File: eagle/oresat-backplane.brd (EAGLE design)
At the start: 82 x 213.6 mm, 98 parts

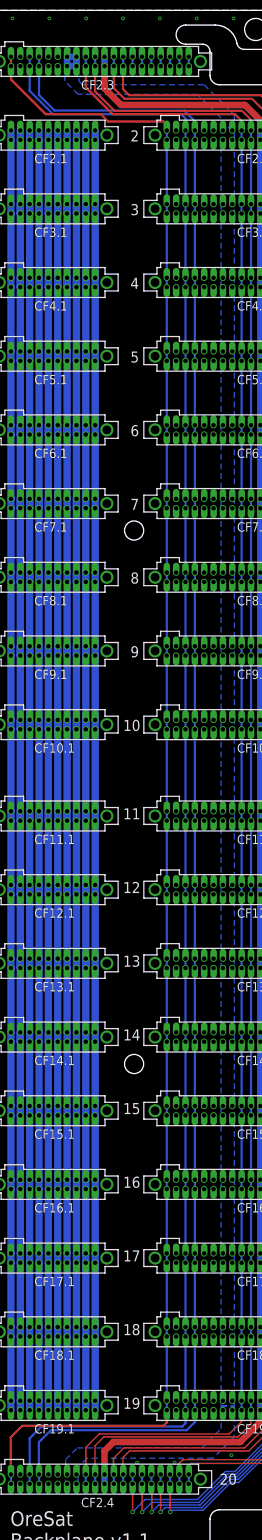
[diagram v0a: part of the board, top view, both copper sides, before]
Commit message: Fixed wrong signal names, removed thermals from bottom of main connectors, should be ready for fab.
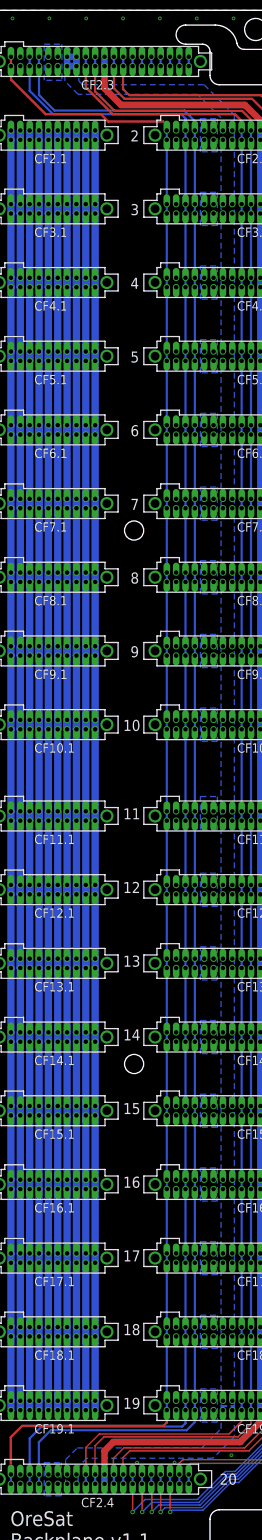
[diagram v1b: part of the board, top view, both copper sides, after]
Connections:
- net MAIN-1 renamed SPARE7
- net MAIN-2 renamed SPARE6
- net MAIN-3 renamed SPARE5
- net MAIN-4 renamed SPARE4
- net MAIN-5 renamed SPARE3
- net MAIN-6 renamed SPARE2
- net MAIN-7 renamed SPARE1
- net PE_PWR renamed OPD_PWR
- net PE_SCL renamed OPD_SCL
- net PE_SDA renamed OPD_SDA
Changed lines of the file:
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@@
 <?xml version="1.0" encoding="utf-8"?>
 <!DOCTYPE eagle SYSTEM "eagle.dtd">
-<eagle version="9.2.2">
+<eagle version="9.3.0">
 <drawing>
 <settings>
-<setting alwaysvectorfont="no"/>
+<setting alwaysvectorfont="yes"/>
 <setting keepoldvectorfont="yes"/>
 <setting verticaltext="up"/>
 </settings>
-<grid distance="1" unitdist="mm" unit="mm" style="lines" multiple="1" display="yes" altdistance="0.025" altunitdist="inch" altunit="inch"/>
+<grid distance="0.1" unitdist="mm" unit="mm" style="lines" multiple="1" display="yes" altdistance="0.025" altunitdist="inch" altunit="inch"/>
 <layers>
-<layer number="1" name="Top" color="4" fill="1" visible="no" active="yes"/>
+<layer number="1" name="Top" color="4" fill="1" visible="yes" active="yes"/>
 <layer number="2" name="Route2" color="1" fill="3" visible="no" active="no"/>
 <layer number="3" name="Route3" color="4" fill="3" visible="no" active="no"/>
@@
 <layer number="14" name="Route14" color="1" fill="6" visible="no" active="no"/>
 <layer number="15" name="Route15" color="4" fill="6" visible="no" active="no"/>
-<layer number="16" name="Bottom" color="1" fill="1" visible="yes" active="yes"/>
+<layer number="16" name="Bottom" color="1" fill="1" visible="no" active="yes"/>
 <layer number="17" name="Pads" color="2" fill="1" visible="yes" active="yes"/>
 <layer number="18" name="Vias" color="2" fill="1" visible="yes" active="yes"/>
 <layer number="19" name="Unrouted" color="6" fill="1" visible="yes" active="yes"/>
 <layer number="20" name="Dimension" color="24" fill="1" visible="yes" active="yes"/>
-<layer number="21" name="tPlace" color="7" fill="1" visible="no" active="yes"/>
-<layer number="22" name="bPlace" color="7" fill="1" visible="yes" active="yes"/>
-<layer number="23" name="tOrigins" color="15" fill="1" visible="no" active="yes"/>
-<layer number="24" name="bOrigins" color="15" fill="1" visible="yes" active="yes"/>
-<layer number="25" name="tNames" color="7" fill="1" visible="no" active="yes"/>
-<layer number="26" name="bNames" color="7" fill="1" visible="yes" active="yes"/>
+<layer number="21" name="tPlace" color="7" fill="1" visible="yes" active="yes"/>
+<layer number="22" name="bPlace" color="7" fill="1" visible="no" active="yes"/>
+<layer number="23" name="tOrigins" color="15" fill="1" visible="yes" active="yes"/>
+<layer number="24" name="bOrigins" color="15" fill="1" visible="no" active="yes"/>
+<layer number="25" name="tNames" color="7" fill="1" visible="yes" active="yes"/>
+<layer number="26" name="bNames" color="7" fill="1" visible="no" active="yes"/>
 <layer number="27" name="tValues" color="7" fill="1" visible="no" active="yes"/>
 <layer number="28" name="bValues" color="7" fill="1" visible="no" active="yes"/>
-<layer number="29" name="tStop" color="7" fill="3" visible="no" active="yes"/>
-<layer number="30" name="bStop" color="7" fill="6" visible="yes" active="yes"/>
+<layer number="29" name="tStop" color="7" fill="3" visible="yes" active="yes"/>
+<layer number="30" name="bStop" color="7" fill="6" visible="no" active="yes"/>
 <layer number="31" name="tCream" color="7" fill="4" visible="no" active="yes"/>
 <layer number="32" name="bCream" color="7" fill="5" visible="no" active="yes"/>
@@
 <via x="1" y="103" extent="1-16" drill="0.254"/>
 <via x="1" y="109" extent="1-16" drill="0.254"/>
+<polygon width="0.2" layer="16" isolate="0.2" thermals="no">
+<vertex x="12.3" y="209"/>
+<vertex x="14.7" y="209"/>
+<vertex x="14.7" y="204.1"/>
+<vertex x="12.3" y="204.1"/>
+</polygon>
+<polygon width="0.2" layer="16" isolate="0.2" thermals="no">
+<vertex x="33.5" y="198.9"/>
+<vertex x="35.8" y="198.9"/>
+<vertex x="35.8" y="194.4"/>
+<vertex x="33.5" y="194.4"/>
+</polygon>
+<polygon width="0.2" layer="16" isolate="0.2" thermals="no">
+<vertex x="33.5" y="188.9"/>
+<vertex x="35.8" y="188.9"/>
+<vertex x="35.8" y="184.4"/>
+<vertex x="33.5" y="184.4"/>
+</polygon>
+<polygon width="0.2" layer="16" isolate="0.2" thermals="no">
+<vertex x="33.5" y="178.9"/>
+<vertex x="35.8" y="178.9"/>
+<vertex x="35.8" y="174.4"/>
+<vertex x="33.5" y="174.4"/>
+</polygon>
+<polygon width="0.2" layer="16" isolate="0.2" thermals="no">
+<vertex x="33.5" y="168.9"/>
+<vertex x="35.8" y="168.9"/>
+<vertex x="35.8" y="164.4"/>
+<vertex x="33.5" y="164.4"/>
+</polygon>
+<polygon width="0.2" layer="16" isolate="0.2" thermals="no">
+<vertex x="33.5" y="158.9"/>
+<vertex x="35.8" y="158.9"/>
+<vertex x="35.8" y="154.4"/>
+<vertex x="33.5" y="154.4"/>
+</polygon>
+<polygon width="0.2" layer="16" isolate="0.2" thermals="no">
+<vertex x="33.5" y="148.9"/>
+<vertex x="35.8" y="148.9"/>
+<vertex x="35.8" y="144.4"/>
+<vertex x="33.5" y="144.4"/>
+</polygon>
+<polygon width="0.2" layer="16" isolate="0.2" thermals="no">
+<vertex x="33.5" y="138.9"/>
+<vertex x="35.8" y="138.9"/>
+<vertex x="35.8" y="134.4"/>
+<vertex x="33.5" y="134.4"/>
+</polygon>
+<polygon width="0.2" layer="16" isolate="0.2" thermals="no">
+<vertex x="33.5" y="128.9"/>
+<vertex x="35.8" y="128.9"/>
+<vertex x="35.8" y="124.4"/>
+<vertex x="33.5" y="124.4"/>
+</polygon>
+<polygon width="0.2" layer="16" isolate="0.2" thermals="no">
+<vertex x="33.5" y="118.9"/>
+<vertex x="35.8" y="118.9"/>
+<vertex x="35.8" y="114.4"/>
+<vertex x="33.5" y="114.4"/>
+</polygon>
+<polygon width="0.2" layer="16" isolate="0.2" thermals="no">
+<vertex x="33.5" y="106.9"/>
+<vertex x="35.8" y="106.9"/>
+<vertex x="35.8" y="102.4"/>
+<vertex x="33.5" y="102.4"/>
+</polygon>
+<polygon width="0.2" layer="16" isolate="0.2" thermals="no">
+<vertex x="33.5" y="96.5"/>
+<vertex x="35.8" y="96.5"/>
+<vertex x="35.8" y="92"/>
+<vertex x="33.5" y="92"/>
+</polygon>
+<polygon width="0.2" layer="16" isolate="0.2" thermals="no">
+<vertex x="33.5" y="86.5"/>
+<vertex x="35.8" y="86.5"/>
+<vertex x="35.8" y="82"/>
+<vertex x="33.5" y="82"/>
+</polygon>
+<polygon width="0.2" layer="16" isolate="0.2" thermals="no">
+<vertex x="33.5" y="76.5"/>
+<vertex x="35.8" y="76.5"/>
+<vertex x="35.8" y="72"/>
+<vertex x="33.5" y="72"/>
+</polygon>
+<polygon width="0.2" layer="16" isolate="0.2" thermals="no">
+<vertex x="33.5" y="66.5"/>
+<vertex x="35.8" y="66.5"/>
+<vertex x="35.8" y="62"/>
+<vertex x="33.5" y="62"/>
+</polygon>
+<polygon width="0.2" layer="16" isolate="0.2" thermals="no">
+<vertex x="33.5" y="56.5"/>
+<vertex x="35.8" y="56.5"/>
+<vertex x="35.8" y="52"/>
+<vertex x="33.5" y="52"/>
+</polygon>
+<polygon width="0.2" layer="16" isolate="0.2" thermals="no">
+<vertex x="33.5" y="46.5"/>
+<vertex x="35.8" y="46.5"/>
+<vertex x="35.8" y="42"/>
+<vertex x="33.5" y="42"/>
+</polygon>
+<polygon width="0.2" layer="16" isolate="0.2" thermals="no">
+<vertex x="33.5" y="36.5"/>
+<vertex x="35.8" y="36.5"/>
+<vertex x="35.8" y="32"/>
+<vertex x="33.5" y="32"/>
+</polygon>
+<polygon width="0.2" layer="16" isolate="0.2" thermals="no">
+<vertex x="33.5" y="26.5"/>
+<vertex x="35.8" y="26.5"/>
+<vertex x="35.8" y="22"/>
+<vertex x="33.5" y="22"/>
+</polygon>
+<polygon width="0.2" layer="16" isolate="0.2" thermals="no">
+<vertex x="12.3" y="16.5"/>
+<vertex x="14.6" y="16.5"/>
+<vertex x="14.6" y="12"/>
+<vertex x="12.3" y="12"/>
+</polygon>
 </signal>
 <signal name="AUX-1">
@@
 <wire x1="7.785" y1="177.295" x2="7.785" y2="176.025" width="1" layer="16"/>
 </signal>
-<signal name="MAIN-1">
+<signal name="SPARE7">
 <contactref element="CF2.2" pad="1"/>
 <contactref element="CF2.2" pad="2"/>
@@
 <wire x1="53.065" y1="197.295" x2="31.915" y2="206.025" width="0" layer="19" extent="1-1"/>
 </signal>
-<signal name="MAIN-2">
+<signal name="SPARE6">
 <contactref element="CF2.2" pad="3"/>
 <contactref element="CF2.2" pad="4"/>
@@
 <wire x1="51.795" y1="197.295" x2="30.645" y2="206.025" width="0" layer="19" extent="1-1"/>
 </signal>
-<signal name="MAIN-3">
+<signal name="SPARE5">
 <contactref element="CF2.2" pad="5"/>
 <contactref element="CF2.2" pad="6"/>
@@
 <wire x1="50.525" y1="197.295" x2="29.375" y2="206.025" width="0" layer="19" extent="1-1"/>
 </signal>
-<signal name="MAIN-4">
+<signal name="SPARE4">
 <contactref element="CF2.2" pad="7"/>
 <contactref element="CF2.2" pad="8"/>
@@
 <wire x1="49.255" y1="197.295" x2="28.105" y2="206.025" width="0" layer="19" extent="1-1"/>
 </signal>
-<signal name="MAIN-5">
+<signal name="SPARE3">
 <contactref element="CF2.2" pad="9"/>
 <contactref element="CF2.2" pad="10"/>
@@
 <wire x1="47.985" y1="197.295" x2="26.835" y2="206.025" width="0" layer="19" extent="1-1"/>
 </signal>
-<signal name="MAIN-6">
+<signal name="SPARE2">
 <contactref element="CF2.2" pad="11"/>
 <contactref element="CF2.2" pad="12"/>
@@
 <wire x1="46.715" y1="197.295" x2="25.565" y2="206.025" width="0" layer="19" extent="1-1"/>
 </signal>
-<signal name="MAIN-7">
+<signal name="SPARE1">
 <contactref element="CF2.2" pad="13"/>
 <contactref element="CF2.2" pad="14"/>
@@
 <wire x1="45.445" y1="197.295" x2="24.295" y2="206.025" width="0" layer="19" extent="1-1"/>
 </signal>
-<signal name="PE_SDA">
+<signal name="OPD_SDA">
 <contactref element="CF2.2" pad="15"/>
 <contactref element="CF2.2" pad="16"/>
@@
 <wire x1="23.025" y1="13.625" x2="23.025" y2="14.895" width="0.3" layer="16"/>
 </signal>
-<signal name="PE_SCL">
+<signal name="OPD_SCL">
 <contactref element="CF2.2" pad="17"/>
 <contactref element="CF2.2" pad="18"/>
@@
 <wire x1="21.755" y1="13.625" x2="21.755" y2="14.895" width="0.3" layer="16"/>
 </signal>
-<signal name="PE_PWR">
+<signal name="OPD_PWR">
 <contactref element="CF2.2" pad="19"/>
 <contactref element="CF2.2" pad="20"/>

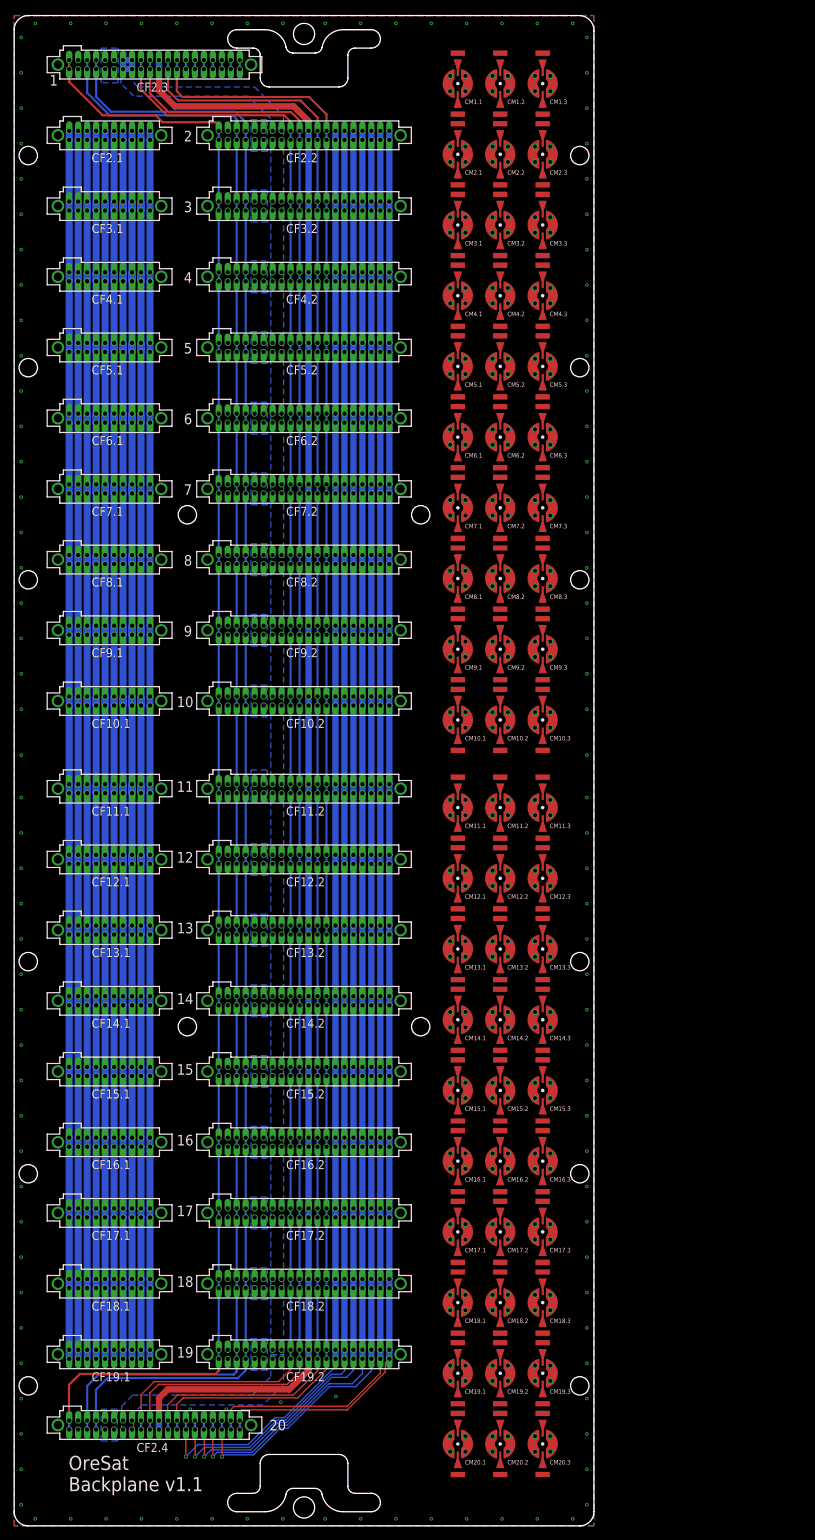
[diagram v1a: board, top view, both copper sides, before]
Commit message: Backplane v3. All good, except for the polygon error that keeps killing EAGLE. I thought this was fixed? Also, the RF stuff is all terrible until Vigely fixgures out what we should do :)
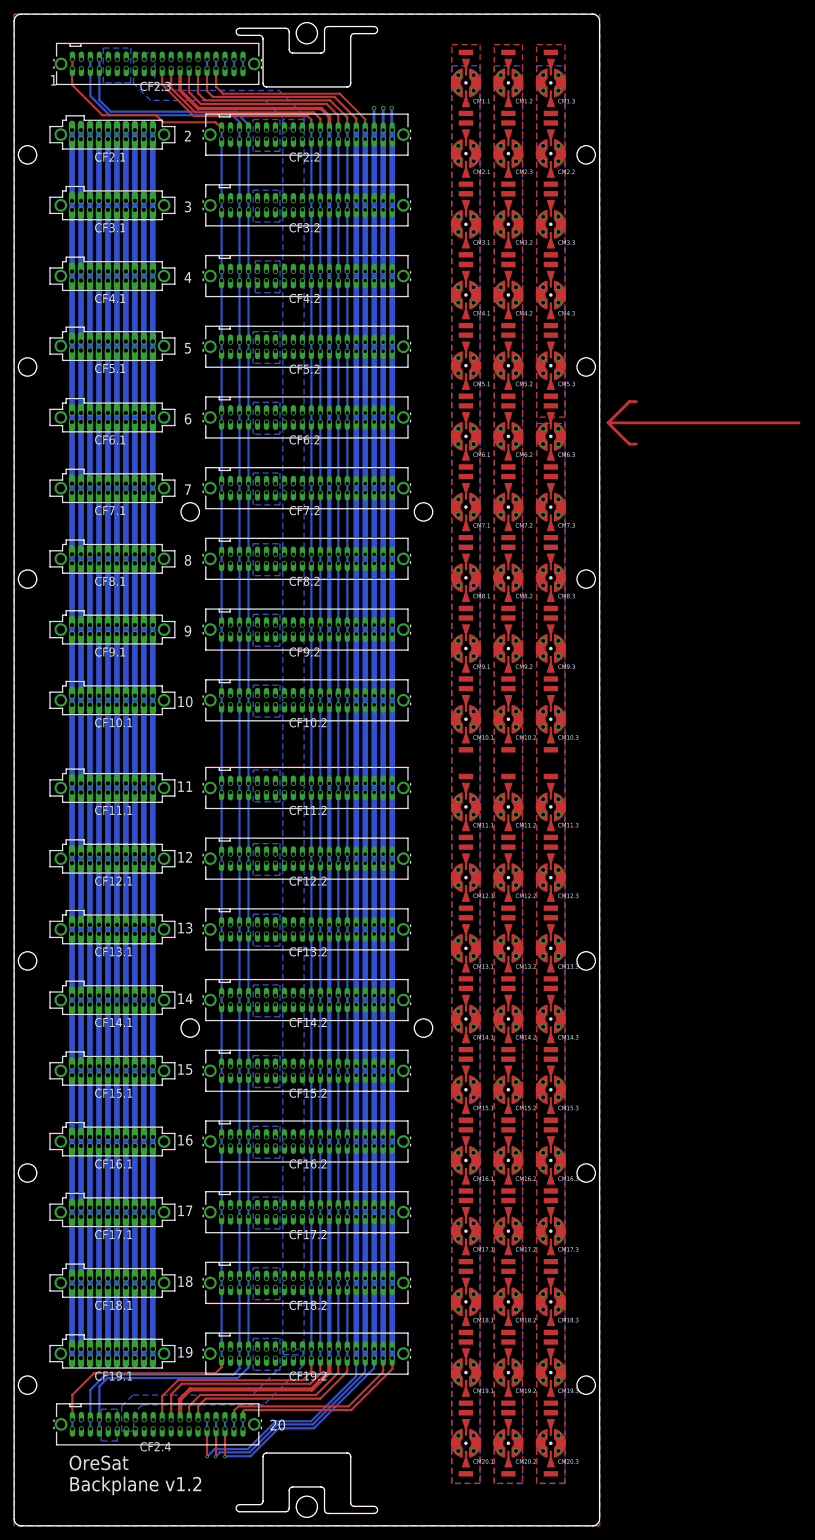
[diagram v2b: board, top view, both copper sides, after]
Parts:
- moved CM2.2 7.15 mm to (75.9, 194.1)
- moved CM2.3 4.85 mm to (69.9, 194.1)
- moved CM1.2 1.15 mm to (69.9, 204.1)
- moved CM1.3 1.15 mm to (75.9, 204.1)
- moved CM3.2 1.15 mm to (69.9, 184.1)
- moved CM3.3 1.15 mm to (75.9, 184.1)
- moved CM4.2 1.15 mm to (69.9, 174.1)
- moved CM4.3 1.15 mm to (75.9, 174.1)
- moved CM5.2 1.15 mm to (69.9, 164.1)
- moved CM5.3 1.15 mm to (75.9, 164.1)
- moved CM6.2 1.15 mm to (69.9, 154.1)
- moved CM6.3 1.15 mm to (75.9, 154.1)
- moved CM7.2 1.15 mm to (69.9, 144.1)
- moved CM7.3 1.15 mm to (75.9, 144.1)
- moved CM8.2 1.15 mm to (69.9, 134.1)
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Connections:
- removed net SPARE6: CF10.2.3, CF10.2.4, CF11.2.3, CF11.2.4, CF12.2.3, CF12.2.4, CF13.2.3, CF13.2.4, CF14.2.3, CF14.2.4, CF15.2.3, CF15.2.4, CF16.2.3, CF16.2.4, CF17.2.3, CF17.2.4, CF18.2.3, CF18.2.4, CF19.2.3, CF19.2.4, CF2.2.3, CF2.2.4, CF2.3.3, CF2.3.4, CF2.4.3, CF2.4.4, CF3.2.3, CF3.2.4, CF4.2.3, CF4.2.4, CF5.2.3, CF5.2.4, CF6.2.3, CF6.2.4, CF7.2.3, CF7.2.4, CF8.2.3, CF8.2.4, CF9.2.3, CF9.2.4
- removed net SPARE7: CF10.2.1, CF10.2.2, CF11.2.1, CF11.2.2, CF12.2.1, CF12.2.2, CF13.2.1, CF13.2.2, CF14.2.1, CF14.2.2, CF15.2.1, CF15.2.2, CF16.2.1, CF16.2.2, CF17.2.1, CF17.2.2, CF18.2.1, CF18.2.2, CF19.2.1, CF19.2.2, CF2.2.1, CF2.2.2, CF2.3.1, CF2.3.2, CF2.4.1, CF2.4.2, CF3.2.1, CF3.2.2, CF4.2.1, CF4.2.2, CF5.2.1, CF5.2.2, CF6.2.1, CF6.2.2, CF7.2.1, CF7.2.2, CF8.2.1, CF8.2.2, CF9.2.1, CF9.2.2
- new net GND1: CM1.1.P$1, CM1.1.P$2, CM1.1.P$3, CM1.1.P$4, CM1.1.P$5, CM1.1.P$6, CM10.1.P$1, CM10.1.P$2, CM10.1.P$3, CM10.1.P$4, CM10.1.P$5, CM10.1.P$6, CM11.1.P$1, CM11.1.P$2, CM11.1.P$3, CM11.1.P$4, CM11.1.P$5, CM11.1.P$6, CM12.1.P$1, CM12.1.P$2, CM12.1.P$3, CM12.1.P$4, CM12.1.P$5, CM12.1.P$6, CM13.1.P$1, CM13.1.P$2, CM13.1.P$3, CM13.1.P$4, CM13.1.P$5, CM13.1.P$6, CM14.1.P$1, CM14.1.P$2, CM14.1.P$3, CM14.1.P$4, CM14.1.P$5, CM14.1.P$6, CM15.1.P$1, CM15.1.P$2, CM15.1.P$3, CM15.1.P$4, CM15.1.P$5, CM15.1.P$6, CM16.1.P$1, CM16.1.P$2, CM16.1.P$3, CM16.1.P$4, CM16.1.P$5, CM16.1.P$6, CM17.1.P$1, CM17.1.P$2, CM17.1.P$3, CM17.1.P$4, CM17.1.P$5, CM17.1.P$6, CM18.1.P$1, CM18.1.P$2, CM18.1.P$3, CM18.1.P$4, CM18.1.P$5, CM18.1.P$6, CM19.1.P$1, CM19.1.P$2, CM19.1.P$3, CM19.1.P$4, CM19.1.P$5, CM19.1.P$6, CM2.1.P$1, CM2.1.P$2, CM2.1.P$3, CM2.1.P$4, CM2.1.P$5, CM2.1.P$6, CM20.1.P$1, CM20.1.P$2, CM20.1.P$3, CM20.1.P$4, CM20.1.P$5, CM20.1.P$6, CM3.1.P$1, CM3.1.P$2, CM3.1.P$3, CM3.1.P$4, CM3.1.P$5, CM3.1.P$6, CM4.1.P$1, CM4.1.P$2, CM4.1.P$3, CM4.1.P$4, CM4.1.P$5, CM4.1.P$6, CM5.1.P$1, CM5.1.P$2, CM5.1.P$3, CM5.1.P$4, CM5.1.P$5, CM5.1.P$6, CM6.1.P$1, CM6.1.P$2, CM6.1.P$3, CM6.1.P$4, CM6.1.P$5, CM6.1.P$6, CM7.1.P$1, CM7.1.P$2, CM7.1.P$3, CM7.1.P$4, CM7.1.P$5, CM7.1.P$6, CM8.1.P$1, CM8.1.P$2, CM8.1.P$3, CM8.1.P$4, CM8.1.P$5, CM8.1.P$6, CM9.1.P$1, CM9.1.P$2, CM9.1.P$3, CM9.1.P$4, CM9.1.P$5, CM9.1.P$6
- new net GND2: CM1.2.P$1, CM1.2.P$2, CM1.2.P$3, CM1.2.P$4, CM1.2.P$5, CM1.2.P$6, CM10.2.P$1, CM10.2.P$2, CM10.2.P$3, CM10.2.P$4, CM10.2.P$5, CM10.2.P$6, CM11.2.P$1, CM11.2.P$2, CM11.2.P$3, CM11.2.P$4, CM11.2.P$5, CM11.2.P$6, CM12.2.P$1, CM12.2.P$2, CM12.2.P$3, CM12.2.P$4, CM12.2.P$5, CM12.2.P$6, CM13.2.P$1, CM13.2.P$2, CM13.2.P$3, CM13.2.P$4, CM13.2.P$5, CM13.2.P$6, CM14.2.P$1, CM14.2.P$2, CM14.2.P$3, CM14.2.P$4, CM14.2.P$5, CM14.2.P$6, CM15.2.P$1, CM15.2.P$2, CM15.2.P$3, CM15.2.P$4, CM15.2.P$5, CM15.2.P$6, CM16.2.P$1, CM16.2.P$2, CM16.2.P$3, CM16.2.P$4, CM16.2.P$5, CM16.2.P$6, CM17.2.P$1, CM17.2.P$2, CM17.2.P$3, CM17.2.P$4, CM17.2.P$5, CM17.2.P$6, CM18.2.P$1, CM18.2.P$2, CM18.2.P$3, CM18.2.P$4, CM18.2.P$5, CM18.2.P$6, CM19.2.P$1, CM19.2.P$2, CM19.2.P$3, CM19.2.P$4, CM19.2.P$5, CM19.2.P$6, CM2.3.P$1, CM2.3.P$2, CM2.3.P$3, CM2.3.P$4, CM2.3.P$5, CM2.3.P$6, CM20.2.P$1, CM20.2.P$2, CM20.2.P$3, CM20.2.P$4, CM20.2.P$5, CM20.2.P$6, CM3.2.P$1, CM3.2.P$2, CM3.2.P$3, CM3.2.P$4, CM3.2.P$5, CM3.2.P$6, CM4.2.P$1, CM4.2.P$2, CM4.2.P$3, CM4.2.P$4, CM4.2.P$5, CM4.2.P$6, CM5.2.P$1, CM5.2.P$2, CM5.2.P$3, CM5.2.P$4, CM5.2.P$5, CM5.2.P$6, CM6.2.P$1, CM6.2.P$2, CM6.2.P$3, CM6.2.P$4, CM6.2.P$5, CM6.2.P$6, CM7.2.P$1, CM7.2.P$2, CM7.2.P$3, CM7.2.P$4, CM7.2.P$5, CM7.2.P$6, CM8.2.P$1, CM8.2.P$2, CM8.2.P$3, CM8.2.P$4, CM8.2.P$5, CM8.2.P$6, CM9.2.P$1, CM9.2.P$2, CM9.2.P$3, CM9.2.P$4, CM9.2.P$5, CM9.2.P$6
- new net GND3: CM1.3.P$1, CM1.3.P$2, CM1.3.P$3, CM1.3.P$4, CM1.3.P$5, CM1.3.P$6, CM10.3.P$1, CM10.3.P$2, CM10.3.P$3, CM10.3.P$4, CM10.3.P$5, CM10.3.P$6, CM11.3.P$1, CM11.3.P$2, CM11.3.P$3, CM11.3.P$4, CM11.3.P$5, CM11.3.P$6, CM12.3.P$1, CM12.3.P$2, CM12.3.P$3, CM12.3.P$4, CM12.3.P$5, CM12.3.P$6, CM13.3.P$1, CM13.3.P$2, CM13.3.P$3, CM13.3.P$4, CM13.3.P$5, CM13.3.P$6, CM14.3.P$1, CM14.3.P$2, CM14.3.P$3, CM14.3.P$4, CM14.3.P$5, CM14.3.P$6, CM15.3.P$1, CM15.3.P$2, CM15.3.P$3, CM15.3.P$4, CM15.3.P$5, CM15.3.P$6, CM16.3.P$1, CM16.3.P$2, CM16.3.P$3, CM16.3.P$4, CM16.3.P$5, CM16.3.P$6, CM17.3.P$1, CM17.3.P$2, CM17.3.P$3, CM17.3.P$4, CM17.3.P$5, CM17.3.P$6, CM18.3.P$1, CM18.3.P$2, CM18.3.P$3, CM18.3.P$4, CM18.3.P$5, CM18.3.P$6, CM19.3.P$1, CM19.3.P$2, CM19.3.P$3, CM19.3.P$4, CM19.3.P$5, CM19.3.P$6, CM2.2.P$1, CM2.2.P$2, CM2.2.P$3, CM2.2.P$4, CM2.2.P$5, CM2.2.P$6, CM20.3.P$1, CM20.3.P$2, CM20.3.P$3, CM20.3.P$4, CM20.3.P$5, CM20.3.P$6, CM3.3.P$1, CM3.3.P$2, CM3.3.P$3, CM3.3.P$4, CM3.3.P$5, CM3.3.P$6, CM4.3.P$1, CM4.3.P$2, CM4.3.P$3, CM4.3.P$4, CM4.3.P$5, CM4.3.P$6, CM5.3.P$1, CM5.3.P$2, CM5.3.P$3, CM5.3.P$4, CM5.3.P$5, CM5.3.P$6, CM6.3.P$1, CM6.3.P$2, CM6.3.P$3, CM6.3.P$4, CM6.3.P$5, CM6.3.P$6, CM7.3.P$1, CM7.3.P$2, CM7.3.P$3, CM7.3.P$4, CM7.3.P$5, CM7.3.P$6, CM8.3.P$1, CM8.3.P$2, CM8.3.P$3, CM8.3.P$4, CM8.3.P$5, CM8.3.P$6, CM9.3.P$1, CM9.3.P$2, CM9.3.P$3, CM9.3.P$4, CM9.3.P$5, CM9.3.P$6
- net CAN2_H: now also CF10.2.17, CF10.2.18, CF11.2.17, CF11.2.18, CF12.2.17, CF12.2.18, CF13.2.17, CF13.2.18, CF14.2.17, CF14.2.18, CF15.2.17, CF15.2.18, CF16.2.17, CF16.2.18, CF17.2.17, CF17.2.18, CF18.2.17, CF18.2.18, CF19.2.17, CF19.2.18, CF2.2.17, CF2.2.18, CF2.3.17, CF2.3.18, CF2.4.17, CF2.4.18, CF3.2.17, CF3.2.18, CF4.2.17, CF4.2.18, CF5.2.17, CF5.2.18, CF6.2.17, CF6.2.18, CF7.2.17, CF7.2.18, CF8.2.17, CF8.2.18, CF9.2.17, CF9.2.18; no longer CF10.2.21, CF10.2.22, CF11.2.21, CF11.2.22, CF12.2.21, CF12.2.22, CF13.2.21, CF13.2.22, CF14.2.21, CF14.2.22, CF15.2.21, CF15.2.22, CF16.2.21, CF16.2.22, CF17.2.21, CF17.2.22, CF18.2.21, CF18.2.22, CF19.2.21, CF19.2.22, CF2.2.21, CF2.2.22, CF2.3.21, CF2.3.22, CF2.4.21, CF2.4.22, CF3.2.21, CF3.2.22, CF4.2.21, CF4.2.22, CF5.2.21, CF5.2.22, CF6.2.21, CF6.2.22, CF7.2.21, CF7.2.22, CF8.2.21, CF8.2.22, CF9.2.21, CF9.2.22
- net CAN2_L: now also CF10.2.19, CF10.2.20, CF11.2.19, CF11.2.20, CF12.2.19, CF12.2.20, CF13.2.19, CF13.2.20, CF14.2.19, CF14.2.20, CF15.2.19, CF15.2.20, CF16.2.19, CF16.2.20, CF17.2.19, CF17.2.20, CF18.2.19, CF18.2.20, CF19.2.19, CF19.2.20, CF2.2.19, CF2.2.20, CF2.3.19, CF2.3.20, CF2.4.19, CF2.4.20, CF3.2.19, CF3.2.20, CF4.2.19, CF4.2.20, CF5.2.19, CF5.2.20, CF6.2.19, CF6.2.20, CF7.2.19, CF7.2.20, CF8.2.19, CF8.2.20, CF9.2.19, CF9.2.20; no longer CF10.2.23, CF10.2.24, CF11.2.23, CF11.2.24, CF12.2.23, CF12.2.24, CF13.2.23, CF13.2.24, CF14.2.23, CF14.2.24, CF15.2.23, CF15.2.24, CF16.2.23, CF16.2.24, CF17.2.23, CF17.2.24, CF18.2.23, CF18.2.24, CF19.2.23, CF19.2.24, CF2.2.23, CF2.2.24, CF2.3.23, CF2.3.24, CF2.4.23, CF2.4.24, CF3.2.23, CF3.2.24, CF4.2.23, CF4.2.24, CF5.2.23, CF5.2.24, CF6.2.23, CF6.2.24, CF7.2.23, CF7.2.24, CF8.2.23, CF8.2.24, CF9.2.23, CF9.2.24
- net GND: now also CF10.2.27, CF10.2.28, CF11.2.27, CF11.2.28, CF12.2.27, CF12.2.28, CF13.2.27, CF13.2.28, CF14.2.27, CF14.2.28, CF15.2.27, CF15.2.28, CF16.2.27, CF16.2.28, CF17.2.27, CF17.2.28, CF18.2.27, CF18.2.28, CF19.2.27, CF19.2.28, CF2.2.27, CF2.2.28, CF2.3.27, CF2.3.28, CF2.4.27, CF2.4.28, CF3.2.27, CF3.2.28, CF4.2.27, CF4.2.28, CF5.2.27, CF5.2.28, CF6.2.27, CF6.2.28, CF7.2.27, CF7.2.28, CF8.2.27, CF8.2.28, CF9.2.27, CF9.2.28; no longer CM1.1.P$1, CM1.1.P$2, CM1.1.P$3, CM1.1.P$4, CM1.1.P$5, CM1.1.P$6, CM1.2.P$1, CM1.2.P$2, CM1.2.P$3, CM1.2.P$4, CM1.2.P$5, CM1.2.P$6, CM1.3.P$1, CM1.3.P$2, CM1.3.P$3, CM1.3.P$4, CM1.3.P$5, CM1.3.P$6, CM10.1.P$1, CM10.1.P$2, CM10.1.P$3, CM10.1.P$4, CM10.1.P$5, CM10.1.P$6, CM10.2.P$1, CM10.2.P$2, CM10.2.P$3, CM10.2.P$4, CM10.2.P$5, CM10.2.P$6, CM10.3.P$1, CM10.3.P$2, CM10.3.P$3, CM10.3.P$4, CM10.3.P$5, CM10.3.P$6, CM11.1.P$1, CM11.1.P$2, CM11.1.P$3, CM11.1.P$4, CM11.1.P$5, CM11.1.P$6, CM11.2.P$1, CM11.2.P$2, CM11.2.P$3, CM11.2.P$4, CM11.2.P$5, CM11.2.P$6, CM11.3.P$1, CM11.3.P$2, CM11.3.P$3, CM11.3.P$4, CM11.3.P$5, CM11.3.P$6, CM12.1.P$1, CM12.1.P$2, CM12.1.P$3, CM12.1.P$4, CM12.1.P$5, CM12.1.P$6, CM12.2.P$1, CM12.2.P$2, CM12.2.P$3, CM12.2.P$4, CM12.2.P$5, CM12.2.P$6, CM12.3.P$1, CM12.3.P$2, CM12.3.P$3, CM12.3.P$4, CM12.3.P$5, CM12.3.P$6, CM13.1.P$1, CM13.1.P$2, CM13.1.P$3, CM13.1.P$4, CM13.1.P$5, CM13.1.P$6, CM13.2.P$1, CM13.2.P$2, CM13.2.P$3, CM13.2.P$4, CM13.2.P$5, CM13.2.P$6, CM13.3.P$1, CM13.3.P$2, CM13.3.P$3, CM13.3.P$4, CM13.3.P$5, CM13.3.P$6, CM14.1.P$1, CM14.1.P$2, CM14.1.P$3, CM14.1.P$4, CM14.1.P$5, CM14.1.P$6, CM14.2.P$1, CM14.2.P$2, CM14.2.P$3, CM14.2.P$4, CM14.2.P$5, CM14.2.P$6, CM14.3.P$1, CM14.3.P$2, CM14.3.P$3, CM14.3.P$4, CM14.3.P$5, CM14.3.P$6, CM15.1.P$1, CM15.1.P$2, CM15.1.P$3, CM15.1.P$4, CM15.1.P$5, CM15.1.P$6, CM15.2.P$1, CM15.2.P$2, CM15.2.P$3, CM15.2.P$4, CM15.2.P$5, CM15.2.P$6, CM15.3.P$1, CM15.3.P$2, CM15.3.P$3, CM15.3.P$4, CM15.3.P$5, CM15.3.P$6, CM16.1.P$1, CM16.1.P$2, CM16.1.P$3, CM16.1.P$4, CM16.1.P$5, CM16.1.P$6, CM16.2.P$1, CM16.2.P$2, CM16.2.P$3, CM16.2.P$4, CM16.2.P$5, CM16.2.P$6, CM16.3.P$1, CM16.3.P$2, CM16.3.P$3, CM16.3.P$4, CM16.3.P$5, CM16.3.P$6, CM17.1.P$1, CM17.1.P$2, CM17.1.P$3, CM17.1.P$4, CM17.1.P$5, CM17.1.P$6, CM17.2.P$1, CM17.2.P$2, CM17.2.P$3, CM17.2.P$4, CM17.2.P$5, CM17.2.P$6, CM17.3.P$1, CM17.3.P$2, CM17.3.P$3, CM17.3.P$4, CM17.3.P$5, CM17.3.P$6, CM18.1.P$1, CM18.1.P$2, CM18.1.P$3, CM18.1.P$4, CM18.1.P$5, CM18.1.P$6, CM18.2.P$1, CM18.2.P$2, CM18.2.P$3, CM18.2.P$4, CM18.2.P$5, CM18.2.P$6, CM18.3.P$1, CM18.3.P$2, CM18.3.P$3, CM18.3.P$4, CM18.3.P$5, CM18.3.P$6, CM19.1.P$1, CM19.1.P$2, CM19.1.P$3, CM19.1.P$4, CM19.1.P$5, CM19.1.P$6, CM19.2.P$1, CM19.2.P$2, CM19.2.P$3, CM19.2.P$4, CM19.2.P$5, CM19.2.P$6, CM19.3.P$1, CM19.3.P$2, CM19.3.P$3, CM19.3.P$4, CM19.3.P$5, CM19.3.P$6, CM2.1.P$1, CM2.1.P$2, CM2.1.P$3, CM2.1.P$4, CM2.1.P$5, CM2.1.P$6, CM2.2.P$1, CM2.2.P$2, CM2.2.P$3, CM2.2.P$4, CM2.2.P$5, CM2.2.P$6, CM2.3.P$1, CM2.3.P$2, CM2.3.P$3, CM2.3.P$4, CM2.3.P$5, CM2.3.P$6, CM20.1.P$1, CM20.1.P$2, CM20.1.P$3, CM20.1.P$4, CM20.1.P$5, CM20.1.P$6, CM20.2.P$1, CM20.2.P$2, CM20.2.P$3, CM20.2.P$4, CM20.2.P$5, CM20.2.P$6, CM20.3.P$1, CM20.3.P$2, CM20.3.P$3, CM20.3.P$4, CM20.3.P$5, CM20.3.P$6, CM3.1.P$1, CM3.1.P$2, CM3.1.P$3, CM3.1.P$4, CM3.1.P$5, CM3.1.P$6, CM3.2.P$1, CM3.2.P$2, CM3.2.P$3, CM3.2.P$4, CM3.2.P$5, CM3.2.P$6, CM3.3.P$1, CM3.3.P$2, CM3.3.P$3, CM3.3.P$4, CM3.3.P$5, CM3.3.P$6, CM4.1.P$1, CM4.1.P$2, CM4.1.P$3, CM4.1.P$4, CM4.1.P$5, CM4.1.P$6, CM4.2.P$1, CM4.2.P$2, CM4.2.P$3, CM4.2.P$4, CM4.2.P$5, CM4.2.P$6, CM4.3.P$1, CM4.3.P$2, CM4.3.P$3, CM4.3.P$4, CM4.3.P$5, CM4.3.P$6, CM5.1.P$1, CM5.1.P$2, CM5.1.P$3, CM5.1.P$4, CM5.1.P$5, CM5.1.P$6, CM5.2.P$1, CM5.2.P$2, CM5.2.P$3, CM5.2.P$4, CM5.2.P$5, CM5.2.P$6, CM5.3.P$1, CM5.3.P$2, CM5.3.P$3, CM5.3.P$4, CM5.3.P$5, CM5.3.P$6, CM6.1.P$1, CM6.1.P$2, CM6.1.P$3, CM6.1.P$4, CM6.1.P$5, CM6.1.P$6, CM6.2.P$1, CM6.2.P$2, CM6.2.P$3, CM6.2.P$4, CM6.2.P$5, CM6.2.P$6, CM6.3.P$1, CM6.3.P$2, CM6.3.P$3, CM6.3.P$4, CM6.3.P$5, CM6.3.P$6, CM7.1.P$1, CM7.1.P$2, CM7.1.P$3, CM7.1.P$4, CM7.1.P$5, CM7.1.P$6, CM7.2.P$1, CM7.2.P$2, CM7.2.P$3, CM7.2.P$4, CM7.2.P$5, CM7.2.P$6, CM7.3.P$1, CM7.3.P$2, CM7.3.P$3, CM7.3.P$4, CM7.3.P$5, CM7.3.P$6, CM8.1.P$1, CM8.1.P$2, CM8.1.P$3, CM8.1.P$4, CM8.1.P$5, CM8.1.P$6, CM8.2.P$1, CM8.2.P$2, CM8.2.P$3, CM8.2.P$4, CM8.2.P$5, CM8.2.P$6, CM8.3.P$1, CM8.3.P$2, CM8.3.P$3, CM8.3.P$4, CM8.3.P$5, CM8.3.P$6, CM9.1.P$1, CM9.1.P$2, CM9.1.P$3, CM9.1.P$4, CM9.1.P$5, CM9.1.P$6, CM9.2.P$1, CM9.2.P$2, CM9.2.P$3, CM9.2.P$4, CM9.2.P$5, CM9.2.P$6, CM9.3.P$1, CM9.3.P$2, CM9.3.P$3, CM9.3.P$4, CM9.3.P$5, CM9.3.P$6
- net OPD_PWR: now also CF10.2.15, CF10.2.16, CF11.2.15, CF11.2.16, CF12.2.15, CF12.2.16, CF13.2.15, CF13.2.16, CF14.2.15, CF14.2.16, CF15.2.15, CF15.2.16, CF16.2.15, CF16.2.16, CF17.2.15, CF17.2.16, CF18.2.15, CF18.2.16, CF19.2.15, CF19.2.16, CF2.2.15, CF2.2.16, CF2.3.15, CF2.3.16, CF2.4.15, CF2.4.16, CF3.2.15, CF3.2.16, CF4.2.15, CF4.2.16, CF5.2.15, CF5.2.16, CF6.2.15, CF6.2.16, CF7.2.15, CF7.2.16, CF8.2.15, CF8.2.16, CF9.2.15, CF9.2.16; no longer CF10.2.19, CF10.2.20, CF11.2.19, CF11.2.20, CF12.2.19, CF12.2.20, CF13.2.19, CF13.2.20, CF14.2.19, CF14.2.20, CF15.2.19, CF15.2.20, CF16.2.19, CF16.2.20, CF17.2.19, CF17.2.20, CF18.2.19, CF18.2.20, CF19.2.19, CF19.2.20, CF2.2.19, CF2.2.20, CF2.3.19, CF2.3.20, CF2.4.19, CF2.4.20, CF3.2.19, CF3.2.20, CF4.2.19, CF4.2.20, CF5.2.19, CF5.2.20, CF6.2.19, CF6.2.20, CF7.2.19, CF7.2.20, CF8.2.19, CF8.2.20, CF9.2.19, CF9.2.20
- net OPD_SCL: now also CF10.2.13, CF10.2.14, CF11.2.13, CF11.2.14, CF12.2.13, CF12.2.14, CF13.2.13, CF13.2.14, CF14.2.13, CF14.2.14, CF15.2.13, CF15.2.14, CF16.2.13, CF16.2.14, CF17.2.13, CF17.2.14, CF18.2.13, CF18.2.14, CF19.2.13, CF19.2.14, CF2.2.13, CF2.2.14, CF2.3.13, CF2.3.14, CF2.4.13, CF2.4.14, CF3.2.13, CF3.2.14, CF4.2.13, CF4.2.14, CF5.2.13, CF5.2.14, CF6.2.13, CF6.2.14, CF7.2.13, CF7.2.14, CF8.2.13, CF8.2.14, CF9.2.13, CF9.2.14; no longer CF10.2.17, CF10.2.18, CF11.2.17, CF11.2.18, CF12.2.17, CF12.2.18, CF13.2.17, CF13.2.18, CF14.2.17, CF14.2.18, CF15.2.17, CF15.2.18, CF16.2.17, CF16.2.18, CF17.2.17, CF17.2.18, CF18.2.17, CF18.2.18, CF19.2.17, CF19.2.18, CF2.2.17, CF2.2.18, CF2.3.17, CF2.3.18, CF2.4.17, CF2.4.18, CF3.2.17, CF3.2.18, CF4.2.17, CF4.2.18, CF5.2.17, CF5.2.18, CF6.2.17, CF6.2.18, CF7.2.17, CF7.2.18, CF8.2.17, CF8.2.18, CF9.2.17, CF9.2.18
- net OPD_SDA: now also CF10.2.11, CF10.2.12, CF11.2.11, CF11.2.12, CF12.2.11, CF12.2.12, CF13.2.11, CF13.2.12, CF14.2.11, CF14.2.12, CF15.2.11, CF15.2.12, CF16.2.11, CF16.2.12, CF17.2.11, CF17.2.12, CF18.2.11, CF18.2.12, CF19.2.11, CF19.2.12, CF2.2.11, CF2.2.12, CF2.3.11, CF2.3.12, CF2.4.11, CF2.4.12, CF3.2.11, CF3.2.12, CF4.2.11, CF4.2.12, CF5.2.11, CF5.2.12, CF6.2.11, CF6.2.12, CF7.2.11, CF7.2.12, CF8.2.11, CF8.2.12, CF9.2.11, CF9.2.12; no longer CF10.2.15, CF10.2.16, CF11.2.15, CF11.2.16, CF12.2.15, CF12.2.16, CF13.2.15, CF13.2.16, CF14.2.15, CF14.2.16, CF15.2.15, CF15.2.16, CF16.2.15, CF16.2.16, CF17.2.15, CF17.2.16, CF18.2.15, CF18.2.16, CF19.2.15, CF19.2.16, CF2.2.15, CF2.2.16, CF2.3.15, CF2.3.16, CF2.4.15, CF2.4.16, CF3.2.15, CF3.2.16, CF4.2.15, CF4.2.16, CF5.2.15, CF5.2.16, CF6.2.15, CF6.2.16, CF7.2.15, CF7.2.16, CF8.2.15, CF8.2.16, CF9.2.15, CF9.2.16
- net SPARE1: now also CF10.2.10, CF10.2.9, CF11.2.10, CF11.2.9, CF12.2.10, CF12.2.9, CF13.2.10, CF13.2.9, CF14.2.10, CF14.2.9, CF15.2.10, CF15.2.9, CF16.2.10, CF16.2.9, CF17.2.10, CF17.2.9, CF18.2.10, CF18.2.9, CF19.2.10, CF19.2.9, CF2.2.10, CF2.2.9, CF2.3.10, CF2.3.9, CF2.4.10, CF2.4.9, CF3.2.10, CF3.2.9, CF4.2.10, CF4.2.9, CF5.2.10, CF5.2.9, CF6.2.10, CF6.2.9, CF7.2.10, CF7.2.9, CF8.2.10, CF8.2.9, CF9.2.10, CF9.2.9; no longer CF10.2.13, CF10.2.14, CF11.2.13, CF11.2.14, CF12.2.13, CF12.2.14, CF13.2.13, CF13.2.14, CF14.2.13, CF14.2.14, CF15.2.13, CF15.2.14, CF16.2.13, CF16.2.14, CF17.2.13, CF17.2.14, CF18.2.13, CF18.2.14, CF19.2.13, CF19.2.14, CF2.2.13, CF2.2.14, CF2.3.13, CF2.3.14, CF2.4.13, CF2.4.14, CF3.2.13, CF3.2.14, CF4.2.13, CF4.2.14, CF5.2.13, CF5.2.14, CF6.2.13, CF6.2.14, CF7.2.13, CF7.2.14, CF8.2.13, CF8.2.14, CF9.2.13, CF9.2.14
- net SPARE2: now also CF10.2.7, CF10.2.8, CF11.2.7, CF11.2.8, CF12.2.7, CF12.2.8, CF13.2.7, CF13.2.8, CF14.2.7, CF14.2.8, CF15.2.7, CF15.2.8, CF16.2.7, CF16.2.8, CF17.2.7, CF17.2.8, CF18.2.7, CF18.2.8, CF19.2.7, CF19.2.8, CF2.2.7, CF2.2.8, CF2.3.7, CF2.3.8, CF2.4.7, CF2.4.8, CF3.2.7, CF3.2.8, CF4.2.7, CF4.2.8, CF5.2.7, CF5.2.8, CF6.2.7, CF6.2.8, CF7.2.7, CF7.2.8, CF8.2.7, CF8.2.8, CF9.2.7, CF9.2.8; no longer CF10.2.11, CF10.2.12, CF11.2.11, CF11.2.12, CF12.2.11, CF12.2.12, CF13.2.11, CF13.2.12, CF14.2.11, CF14.2.12, CF15.2.11, CF15.2.12, CF16.2.11, CF16.2.12, CF17.2.11, CF17.2.12, CF18.2.11, CF18.2.12, CF19.2.11, CF19.2.12, CF2.2.11, CF2.2.12, CF2.3.11, CF2.3.12, CF2.4.11, CF2.4.12, CF3.2.11, CF3.2.12, CF4.2.11, CF4.2.12, CF5.2.11, CF5.2.12, CF6.2.11, CF6.2.12, CF7.2.11, CF7.2.12, CF8.2.11, CF8.2.12, CF9.2.11, CF9.2.12
- net SPARE3: now also CF10.2.5, CF10.2.6, CF11.2.5, CF11.2.6, CF12.2.5, CF12.2.6, CF13.2.5, CF13.2.6, CF14.2.5, CF14.2.6, CF15.2.5, CF15.2.6, CF16.2.5, CF16.2.6, CF17.2.5, CF17.2.6, CF18.2.5, CF18.2.6, CF19.2.5, CF19.2.6, CF2.2.5, CF2.2.6, CF2.3.5, CF2.3.6, CF2.4.5, CF2.4.6, CF3.2.5, CF3.2.6, CF4.2.5, CF4.2.6, CF5.2.5, CF5.2.6, CF6.2.5, CF6.2.6, CF7.2.5, CF7.2.6, CF8.2.5, CF8.2.6, CF9.2.5, CF9.2.6; no longer CF10.2.10, CF10.2.9, CF11.2.10, CF11.2.9, CF12.2.10, CF12.2.9, CF13.2.10, CF13.2.9, CF14.2.10, CF14.2.9, CF15.2.10, CF15.2.9, CF16.2.10, CF16.2.9, CF17.2.10, CF17.2.9, CF18.2.10, CF18.2.9, CF19.2.10, CF19.2.9, CF2.2.10, CF2.2.9, CF2.3.10, CF2.3.9, CF2.4.10, CF2.4.9, CF3.2.10, CF3.2.9, CF4.2.10, CF4.2.9, CF5.2.10, CF5.2.9, CF6.2.10, CF6.2.9, CF7.2.10, CF7.2.9, CF8.2.10, CF8.2.9, CF9.2.10, CF9.2.9
- net SPARE4: now also CF10.2.3, CF10.2.4, CF11.2.3, CF11.2.4, CF12.2.3, CF12.2.4, CF13.2.3, CF13.2.4, CF14.2.3, CF14.2.4, CF15.2.3, CF15.2.4, CF16.2.3, CF16.2.4, CF17.2.3, CF17.2.4, CF18.2.3, CF18.2.4, CF19.2.3, CF19.2.4, CF2.2.3, CF2.2.4, CF2.3.3, CF2.3.4, CF2.4.3, CF2.4.4, CF3.2.3, CF3.2.4, CF4.2.3, CF4.2.4, CF5.2.3, CF5.2.4, CF6.2.3, CF6.2.4, CF7.2.3, CF7.2.4, CF8.2.3, CF8.2.4, CF9.2.3, CF9.2.4; no longer CF10.2.7, CF10.2.8, CF11.2.7, CF11.2.8, CF12.2.7, CF12.2.8, CF13.2.7, CF13.2.8, CF14.2.7, CF14.2.8, CF15.2.7, CF15.2.8, CF16.2.7, CF16.2.8, CF17.2.7, CF17.2.8, CF18.2.7, CF18.2.8, CF19.2.7, CF19.2.8, CF2.2.7, CF2.2.8, CF2.3.7, CF2.3.8, CF2.4.7, CF2.4.8, CF3.2.7, CF3.2.8, CF4.2.7, CF4.2.8, CF5.2.7, CF5.2.8, CF6.2.7, CF6.2.8, CF7.2.7, CF7.2.8, CF8.2.7, CF8.2.8, CF9.2.7, CF9.2.8
- net SPARE5: now also CF10.2.1, CF10.2.2, CF11.2.1, CF11.2.2, CF12.2.1, CF12.2.2, CF13.2.1, CF13.2.2, CF14.2.1, CF14.2.2, CF15.2.1, CF15.2.2, CF16.2.1, CF16.2.2, CF17.2.1, CF17.2.2, CF18.2.1, CF18.2.2, CF19.2.1, CF19.2.2, CF2.2.1, CF2.2.2, CF2.3.1, CF2.3.2, CF2.4.1, CF2.4.2, CF3.2.1, CF3.2.2, CF4.2.1, CF4.2.2, CF5.2.1, CF5.2.2, CF6.2.1, CF6.2.2, CF7.2.1, CF7.2.2, CF8.2.1, CF8.2.2, CF9.2.1, CF9.2.2; no longer CF10.2.5, CF10.2.6, CF11.2.5, CF11.2.6, CF12.2.5, CF12.2.6, CF13.2.5, CF13.2.6, CF14.2.5, CF14.2.6, CF15.2.5, CF15.2.6, CF16.2.5, CF16.2.6, CF17.2.5, CF17.2.6, CF18.2.5, CF18.2.6, CF19.2.5, CF19.2.6, CF2.2.5, CF2.2.6, CF2.3.5, CF2.3.6, CF2.4.5, CF2.4.6, CF3.2.5, CF3.2.6, CF4.2.5, CF4.2.6, CF5.2.5, CF5.2.6, CF6.2.5, CF6.2.6, CF7.2.5, CF7.2.6, CF8.2.5, CF8.2.6, CF9.2.5, CF9.2.6
- net VBUS: now also CF10.2.21, CF10.2.22, CF10.2.23, CF10.2.24, CF11.2.21, CF11.2.22, CF11.2.23, CF11.2.24, CF12.2.21, CF12.2.22, CF12.2.23, CF12.2.24, CF13.2.21, CF13.2.22, CF13.2.23, CF13.2.24, CF14.2.21, CF14.2.22, CF14.2.23, CF14.2.24, CF15.2.21, CF15.2.22, CF15.2.23, CF15.2.24, CF16.2.21, CF16.2.22, CF16.2.23, CF16.2.24, CF17.2.21, CF17.2.22, CF17.2.23, CF17.2.24, CF18.2.21, CF18.2.22, CF18.2.23, CF18.2.24, CF19.2.21, CF19.2.22, CF19.2.23, CF19.2.24, CF2.2.21, CF2.2.22, CF2.2.23, CF2.2.24, CF2.3.21, CF2.3.22, CF2.3.23, CF2.3.24, CF2.4.21, CF2.4.22, CF2.4.23, CF2.4.24, CF3.2.21, CF3.2.22, CF3.2.23, CF3.2.24, CF4.2.21, CF4.2.22, CF4.2.23, CF4.2.24, CF5.2.21, CF5.2.22, CF5.2.23, CF5.2.24, CF6.2.21, CF6.2.22, CF6.2.23, CF6.2.24, CF7.2.21, CF7.2.22, CF7.2.23, CF7.2.24, CF8.2.21, CF8.2.22, CF8.2.23, CF8.2.24, CF9.2.21, CF9.2.22, CF9.2.23, CF9.2.24; no longer CF10.2.27, CF10.2.28, CF11.2.27, CF11.2.28, CF12.2.27, CF12.2.28, CF13.2.27, CF13.2.28, CF14.2.27, CF14.2.28, CF15.2.27, CF15.2.28, CF16.2.27, CF16.2.28, CF17.2.27, CF17.2.28, CF18.2.27, CF18.2.28, CF19.2.27, CF19.2.28, CF2.2.27, CF2.2.28, CF2.3.27, CF2.3.28, CF2.4.27, CF2.4.28, CF3.2.27, CF3.2.28, CF4.2.27, CF4.2.28, CF5.2.27, CF5.2.28, CF6.2.27, CF6.2.28, CF7.2.27, CF7.2.28, CF8.2.27, CF8.2.28, CF9.2.27, CF9.2.28
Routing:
- net SPARE6: track 203.1 -> 0.00 mm
- net SPARE7: track 202.4 -> 0.00 mm
- net N$1: track 0.00 -> 37.5 mm
- net SPARE1: track 207.5 -> 236.0 mm
- net SPARE2: track 207.9 -> 235.4 mm
- net VBUS: track 5.08 -> 0.00 mm
- net SPARE3: track 207.8 -> 211.0 mm, vias 1 -> 2
- net CAN2_H: track 232.0 -> 229.1 mm
- net CAN2_L: track 231.2 -> 228.4 mm
- net OPD_SCL: track 231.0 -> 228.6 mm
- net OPD_PWR: track 231.1 -> 228.9 mm
- net SPARE5: track 207.9 -> 205.7 mm
- net SPARE4: track 208.1 -> 205.9 mm
- net OPD_SDA: track 231.2 -> 229.8 mm
- net AUX-4: track 183.8 -> 182.6 mm
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- added copper zone on layer 1, net GND1
- added copper zone on layer 16, net GND1
- added copper zone on layer 1, net GND2
- added copper zone on layer 16, net GND2
- added copper zone on layer 1, net GND3
- added copper zone on layer 16, net GND3
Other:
- board size 82 x 213.6 mm -> 82.8 x 213.8 mm
- board text added: "Backplane v1.2"
- board text added: "OreSat Backplane v1.2"
- board text removed: "Backplane v1.1"
- board text removed: "OreSat Backplane v1.1"
